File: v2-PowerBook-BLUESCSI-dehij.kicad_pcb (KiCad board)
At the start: 2 copper layers, 96.5 x 50.8 mm, 44 parts, among them J1 Micro_SD_Card, J2 Conn_02x20_Odd_Even, U1 YAAJ_BluePill_Part_Like

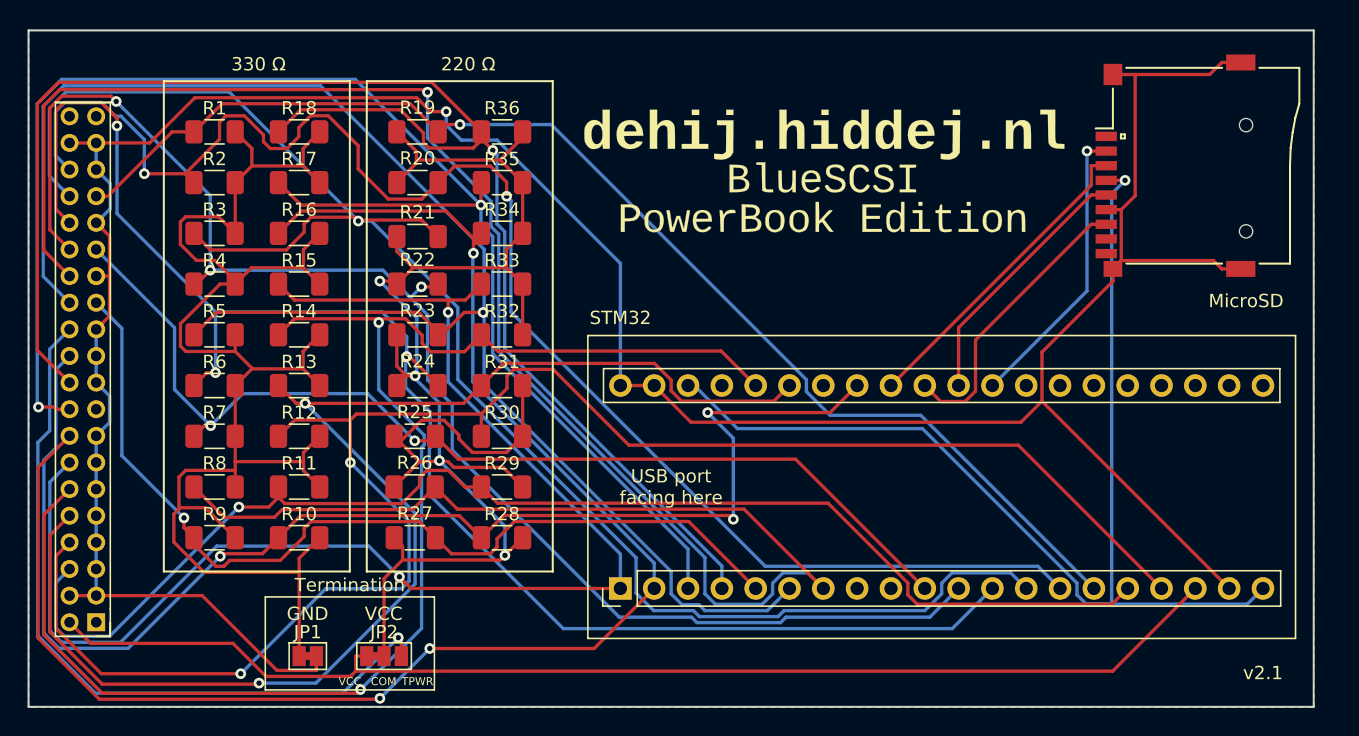
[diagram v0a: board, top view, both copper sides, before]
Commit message: Moved resistors to 2 lines added silk screen rounded corners changed sd card
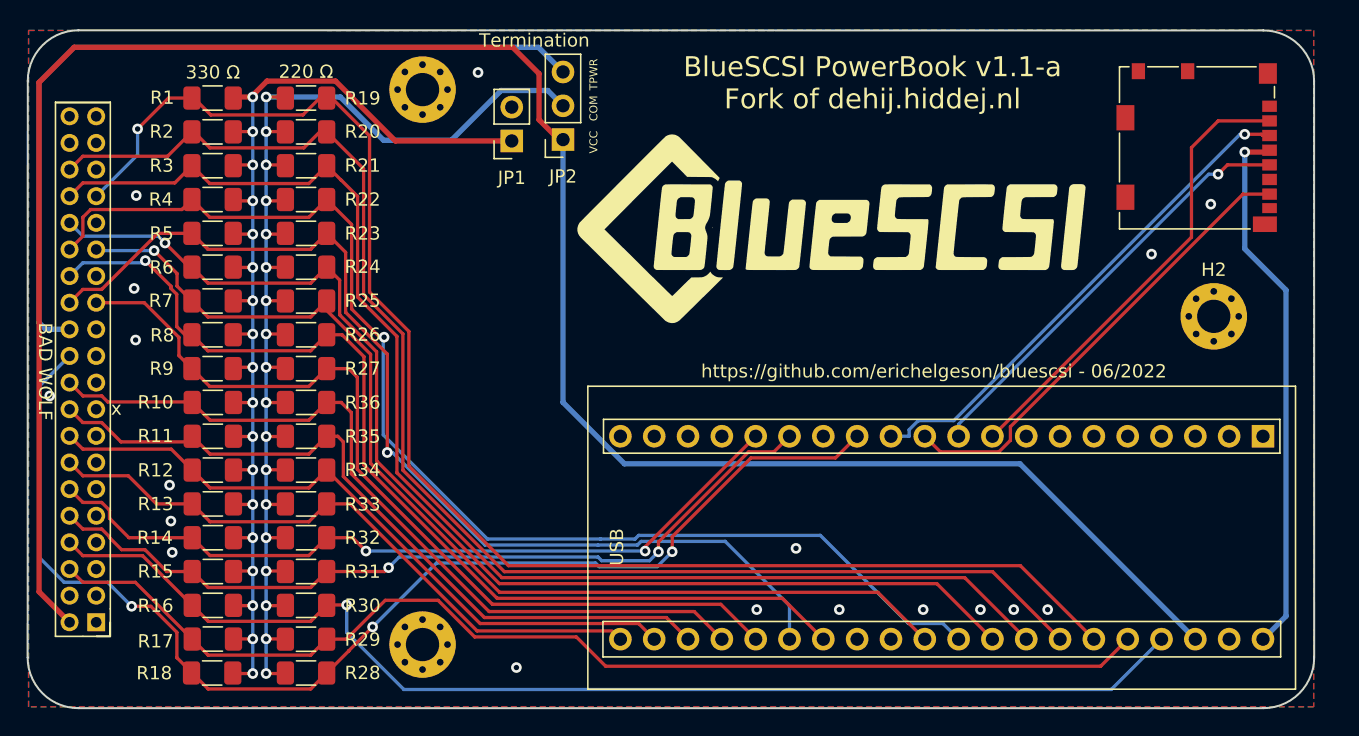
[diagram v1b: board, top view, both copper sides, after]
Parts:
- removed G1: LOGO, Other footprints:Backsilkscreen
- removed G2: LOGO, Other footprints:PBlogo2
- removed REF**: OSHW-Logo_7.5x8mm_SilkScreen, Symbol:OSHW-Logo_7.5x8mm_SilkScreen
- added G***: LOGO, LOGO, F.Cu at (134.0, 91.0)
- added G***: LOGO, LOGO, B.Cu at (121.0, 92.0)
- added G***: LOGO, LOGO, B.Cu at (91.0, 118.0)
- added H1: MountingHole_Pad, MountingHole:MountingHole_2.5mm_Pad_Via, F.Cu at (103.2, 122.3)
- added H2: MountingHole_Pad, MountingHole:MountingHole_2.5mm_Pad_Via, F.Cu at (162.7, 97.7)
- added H3: MountingHole_Pad, MountingHole:MountingHole_2.5mm_Pad_Via, F.Cu at (103.2, 80.6)
- J1: footprint Other footprints:Conn_uSDcard -> Connector_Card:microSD_HC_Molex_104031-0811
- JP1: footprint Jumper:SolderJumper-2_P1.3mm_Bridged_Pad1.0x1.5mm -> Connector_PinSocket_2.54mm:PinSocket_1x02_P2.54mm_Vertical
- JP2: footprint Jumper:SolderJumper-3_P1.3mm_Bridged12_Pad1.0x1.5mm_NumberLabels -> Connector_PinSocket_2.54mm:PinSocket_1x03_P2.54mm_Vertical
- moved JP1 41.6 mm to (110.0, 84.5), turned to 180 degrees
- moved R18 41.2 mm to (87.5, 124.5)
- moved JP2 41.1 mm to (113.8, 84.4), turned to 180 degrees
- moved R17 34.9 mm to (87.5, 121.9)
- moved R16 28.7 mm to (87.5, 119.4)
- moved R36 25.1 mm to (94.5, 104.1), turned to 0 degrees
- moved R35 24.1 mm to (94.5, 106.7), turned to 0 degrees
- moved R34 23.1 mm to (94.5, 109.2), turned to 0 degrees
- moved R15 22.5 mm to (87.5, 116.8)
- moved R33 22.1 mm to (94.5, 111.8), turned to 0 degrees
- moved R32 21.2 mm to (94.5, 114.3), turned to 0 degrees
- moved R31 20.3 mm to (94.5, 116.8), turned to 0 degrees
- moved R30 19.4 mm to (94.5, 119.4), turned to 0 degrees
- moved R29 18.6 mm to (94.5, 121.9), turned to 0 degrees
- moved R28 17.9 mm to (94.5, 124.5), turned to 0 degrees
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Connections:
- J1 pad 1: Net-(J1-Pad1) -> unconnected-(J1-Pad1)
- J1 pad 8: Net-(J1-Pad8) -> unconnected-(J1-Pad8)
- J1 pad 9: Net-(J1-Pad9) -> unconnected-(J1-Pad9)
- J2 pad 1: Net-(J2-Pad1) -> unconnected-(J2-Pad1)
- J2 pad 17: Net-(J2-Pad17) -> unconnected-(J2-Pad17)
- J2 pad 39: Net-(J2-Pad39) -> unconnected-(J2-Pad39)
- J2 pad 40: Net-(J2-Pad40) -> unconnected-(J2-Pad40)
- R10 pad 2: /SCSI_DBP -> /SCSI_DAT7
- R11 pad 2: /SCSI_DAT0 -> /SCSI_DAT6
- R12 pad 2: /SCSI_DAT1 -> /SCSI_DAT5
- R13 pad 2: /SCSI_DAT2 -> /SCSI_DAT4
- R15 pad 2: /SCSI_DAT4 -> /SCSI_DAT2
- R16 pad 2: /SCSI_DAT5 -> /SCSI_DAT1
- R17 pad 2: /SCSI_DAT6 -> /SCSI_DAT0
- R18 pad 2: /SCSI_DAT7 -> /SCSI_DBP
- U1 pad 21: Net-(U1-Pad21) -> unconnected-(U1-Pad21)
- U1 pad 22: Net-(U1-Pad22) -> unconnected-(U1-Pad22)
- U1 pad 23: Net-(U1-Pad23) -> unconnected-(U1-Pad23)
- U1 pad 24: Net-(U1-Pad24) -> unconnected-(U1-Pad24)
- U1 pad 25: Net-(U1-Pad25) -> unconnected-(U1-Pad25)
- U1 pad 26: Net-(U1-Pad26) -> unconnected-(U1-Pad26)
- U1 pad 27: Net-(U1-Pad27) -> unconnected-(U1-Pad27)
- U1 pad 28: Net-(U1-Pad28) -> unconnected-(U1-Pad28)
- U1 pad 34: Net-(U1-Pad34) -> unconnected-(U1-Pad34)
- U1 pad 37: Net-(U1-Pad37) -> unconnected-(U1-Pad37)
- U1 pad 38: +3V3 -> unconnected-(U1-Pad38)
- U1 pad 8: Net-(U1-Pad8) -> unconnected-(U1-Pad8)
- U1 pad 9: Net-(U1-Pad9) -> unconnected-(U1-Pad9)
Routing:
- net GND: track 218.3 -> 0.00 mm, vias 1 -> 18
- net /SCSI_ACK: track 152.8 -> 75.6 mm
- net VCC: track 90.9 -> 161.1 mm
- net /SCSI_DAT5: track 116.7 -> 51.3 mm, vias 3 -> 0
- net /SCSI_DAT6: track 116.1 -> 56.0 mm, vias 2 -> 0
- net /SCSI_DAT4: track 104.0 -> 47.1 mm, vias 2 -> 0
- net /SCSI_DAT7: track 117.1 -> 60.7 mm, vias 1 -> 0
- net /SCSI_DAT3: track 108.5 -> 58.7 mm
- net +3V3: track 84.6 -> 40.3 mm
- net /SCSI_BSY: track 120.1 -> 78.5 mm
- net /SCSI_DAT1: track 129.0 -> 89.9 mm, vias 2 -> 1
- net /SCSI_DAT2: track 100.8 -> 61.7 mm
- net /SCSI_SEL: track 117.2 -> 89.6 mm, vias 3 -> 1
- net /SCSI_CD: track 125.4 -> 99.1 mm, vias 1 -> 0
- net Net-(JP1-Pad1): track 116.7 -> 90.4 mm, vias 0 -> 18
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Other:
- board size 96.5 x 50.8 mm -> 96.6 x 50.9 mm
- board text added: "BAD WOLF"
- board text added: "BlueSCSI PowerBook v1.1-a Fork of dehij.hiddej.nl"
- board text added: "USB"
- board text added: "https://github.com/erichelgeson/bluescsi - 06/2022"
- board text added: "x"
- board text removed: "01-2022"
- board text removed: "GND"
- board text removed: "MicroSD"
- board text removed: "STM32"
- board text removed: "USB port facing here"
- board text removed: "v2.1"

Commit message: Tonys Updates
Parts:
- J1: footprint Connector_Card:microSD_HC_Molex_104031-0811 -> Other footprints:3d_MODEL_microSD_HC_Molex_104031-0811
- R1, R10, R11, R12, R13, R14, R15, R16, R17, R18, R2, R3, R4, R5, R6, R7, R8, R9: value R -> 330
- R19, R20, R21, R22, R23, R24, R25, R26, R27, R28, R29, R30, R31, R32, R33, R34, R35, R36: value R -> 220
- U1: footprint Footprints:YAAJ_BluePill_2 -> Footprints:YAAJ_BluePill_1
- moved G*** 37.2 mm to (147.1, 118.4)
- moved G*** 29.2 mm to (143.6, 118.6)
- moved U1 19.9 mm to (102.8, 109.3)
- turned J1 to 90 degrees
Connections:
- H1 pad 1: unconnected-(H1-Pad1) -> GND
- H2 pad 1: unconnected-(H2-Pad1) -> GND
- H3 pad 1: unconnected-(H3-Pad1) -> GND
- J1 pad 9: unconnected-(J1-Pad9) -> GND
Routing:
- net /SCSI_DAT6: track 56.0 -> 35.6 mm, vias 0 -> 1
- net /SCSI_ATN: track 66.0 -> 45.6 mm, vias 0 -> 1
- net /SCSI_DAT7: track 60.7 -> 40.6 mm, vias 0 -> 1
- net /SCSI_DAT5: track 51.3 -> 31.7 mm
- net /SCSI_ACK: track 75.6 -> 56.3 mm, vias 1 -> 2
- net /SCSI_RST: track 80.4 -> 61.6 mm, vias 1 -> 2
- net /SCSI_CD: track 99.1 -> 81.0 mm, vias 0 -> 1
- net /SCSI_DAT4: track 47.1 -> 29.5 mm
- net /SCSI_IO: track 108.8 -> 91.7 mm, vias 1 -> 2
- net /SCSI_BSY: track 78.5 -> 61.7 mm
- net /SCSI_REQ: track 103.2 -> 86.5 mm, vias 0 -> 1
- net VCC: track 161.1 -> 144.7 mm, vias 0 -> 1
- net /SCSI_MSG: track 92.3 -> 76.1 mm
- net /SCSI_SEL: track 89.6 -> 75.5 mm, vias 1 -> 2
- net +3V3: track 40.3 -> 28.3 mm
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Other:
- board text added: "09/2022"
- board text added: "BlueSCSI PowerBook v1.1-a+ Fork of dehij.hiddej.nl Updates by E. Helgeson & A. Kuker"
- board text added: "https://github.com/erichelgeson/bluescsi"
- board text removed: "BlueSCSI PowerBook v1.1-a Fork of dehij.hiddej.nl"
- board text removed: "USB"
- board text removed: "https://github.com/erichelgeson/bluescsi - 06/2022"
